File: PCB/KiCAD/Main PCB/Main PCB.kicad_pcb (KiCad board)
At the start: 2 copper layers, 120 x 120 mm, 144 parts, among them IC1 ADG608BRZ, IC2 ADG608BRZ, IC3 XB3-24Z8CM, J1 Conn_01x02, J2 Conn_01x02, J3 Conn_01x02, J4 Conn_Coaxial_Small, J5 Conn_01x02, J6 Conn_01x04, J7 Conn_01x04, M1 Conn_01x02_Pin, M2 Conn_01x02_Pin, M3 Conn_01x02_Pin, M4 Conn_01x02_Pin, Q1 BSS138, Q2 BSS138, U2 Teensy4.1, U3 Teensy4.0, U4 LMD18200, U5 LMD18200, U6 LMD18200, U7 LMD18200, U8 MIC5219-3.3YM5

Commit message: Updated to main PCB
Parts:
- added J8: Conn_01x04, Connector_JST:JST_PH_B4B-PH-K_1x04_P2.00mm_Vertical, F.Cu at (29.0, 14.5)
- turned D10 to 158 degrees
- turned D12 to 113 degrees
- turned D14 to 68 degrees
- turned D16 to 23 degrees
- turned D18 to -22 degrees
- turned D20 to -67 degrees
- turned D22 to -112 degrees
- turned D24 to -157 degrees
- turned IR10 to -22 degrees
- turned IR12 to -67 degrees
- turned IR14 to -112 degrees
- turned IR16 to -157 degrees
- turned IR2 to 158 degrees
- turned IR4 to 113 degrees
- turned IR6 to 68 degrees
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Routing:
- net GND: track 77.1 -> 964.7 mm, vias 0 -> 1
- net TSSP_PWR: track 0.00 -> 410.8 mm, vias 0 -> 4
- net +3V3: track 0.00 -> 215.3 mm, vias 0 -> 6
- net +5V: track 0.00 -> 163.3 mm, vias 0 -> 3
- net IR_DIR_157.5: track 0.00 -> 158.9 mm, vias 0 -> 3
- net LG_RECEIVE: track 0.00 -> 154.4 mm, vias 0 -> 6
- net +3V3_4_0: track 0.00 -> 147.1 mm, vias 0 -> 8
- net START_BUTTON: track 0.00 -> 137.2 mm, vias 0 -> 2
- net LED_2_A2: track 0.00 -> 134.7 mm, vias 0 -> 2
- net +3V3_4_1: track 0.00 -> 132.3 mm, vias 0 -> 5
- net 3V3_SDA: track 0.00 -> 125.4 mm, vias 0 -> 3
- net IR_DIR_180: track 0.00 -> 119.8 mm, vias 0 -> 4
- net IR_DIR_112.5: track 0.00 -> 119.7 mm, vias 0 -> 1
- net 3V3_SCL: track 0.00 -> 114.6 mm, vias 0 -> 4
- net CAMERA_TX: track 0.00 -> 109.3 mm, vias 0 -> 3
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- removed copper zone on B.Cu, net GND
- removed copper zone on F.Cu, net GND

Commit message: More PCB updates
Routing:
- net START_BUTTON: track 137.2 -> 136.2 mm
- net Net-(IC1-S1): track 55.2 -> 55.9 mm
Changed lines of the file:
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@@
 	)
 	(segment
-		(start -6.6409 7.9077)
-		(end -6.7522 8.019)
+		(start -6.75 7.75)
+		(end -7 8)
 		(width 0.2)
 		(layer "F.Cu")
@@
 	)
 	(segment
-		(start -4.8253 15.3253)
-		(end -3.75 14.25)
+		(start -4.8253 27.3847)
+		(end -4.8253 15.3253)
 		(width 0.2)
 		(layer "F.Cu")
@@
 	)
 	(segment
-		(start -3.75 14.25)
-		(end -3.75 9.0079)
+		(start -6.77 9.73)
+		(end -7 9.5)
 		(width 0.2)
 		(layer "F.Cu")
@@
 	)
 	(segment
-		(start -4.8253 27.3847)
-		(end -4.8253 15.3253)
+		(start 2.54 54.55)
+		(end 2.54 34.75)
 		(width 0.2)
 		(layer "F.Cu")
@@
 	)
 	(segment
-		(start -6.7522 9.73)
-		(end -5.788 9.73)
+		(start 2.54 34.75)
+		(end -4.8253 27.3847)
 		(width 0.2)
 		(layer "F.Cu")
@@
 	)
 	(segment
-		(start -4.8502 7.9077)
-		(end -6.6409 7.9077)
+		(start -3.75 8.75)
+		(end -4.75 7.75)
 		(width 0.2)
 		(layer "F.Cu")
@@
 	)
 	(segment
-		(start -3.75 9.0079)
-		(end -4.8502 7.9077)
+		(start -5.788 9.73)
+		(end -6.77 9.73)
 		(width 0.2)
 		(layer "F.Cu")
@@
 	)
 	(segment
-		(start 2.54 34.75)
-		(end -4.8253 27.3847)
+		(start -3.75 14.25)
+		(end -3.75 8.75)
 		(width 0.2)
 		(layer "F.Cu")
@@
 	)
 	(segment
-		(start 2.54 54.55)
-		(end 2.54 34.75)
+		(start -7 8)
+		(end -7 9.5)
+		(width 0.2)
+		(layer "F.Cu")
+		(net 17)
+	)
+	(segment
+		(start -4.8253 15.3253)
+		(end -3.75 14.25)
 		(width 0.2)
 		(layer "F.Cu")
@@
 	)
 	(segment
-		(start -6.7522 8.019)
-		(end -6.7522 9.73)
+		(start -4.75 7.75)
+		(end -6.75 7.75)
 		(width 0.2)
 		(layer "F.Cu")
@@
 	)
 	(segment
-		(start 9.6074 -6.0644)
-		(end 9.6074 -3.5)
+		(start 13.44 6)
+		(end 9.6074 6)
 		(width 0.2)
 		(layer "B.Cu")
@@
 	)
 	(segment
-		(start 10.3933 6.7859)
-		(end 9.6074 6)
+		(start 9.6074 -6.0644)
+		(end 9.6074 -3.5)
 		(width 0.2)
 		(layer "B.Cu")
@@
 	)
 	(segment
-		(start 14.2259 6.7859)
-		(end 10.3933 6.7859)
+		(start 17.75 -48.6127)
+		(end 17.8099 -48.6726)
 		(width 0.2)
 		(layer "B.Cu")
@@
 	(segment
 		(start 15.75 8.31)
-		(end 14.2259 6.7859)
-		(width 0.2)
-		(layer "B.Cu")
-		(net 54)
-	)
-	(segment
-		(start 17.75 -48.6127)
-		(end 17.8099 -48.6726)
+		(end 13.44 6)
 		(width 0.2)
 		(layer "B.Cu")
@@
 	)
 	(segment
-		(start -23.4375 11.0625)
-		(end -19.5 11.0625)
-		(width 0.68)
-		(layer "B.Cu")
-		(net 70)
-	)
-	(segment
-		(start -24.7 9.8)
-		(end -23.4375 11.0625)
+		(start -37.5 11)
+		(end -39.5 13)
 		(width 0.68)
 		(layer "B.Cu")
@@
 	)
 	(segment
-		(start -37.5 11)
-		(end -39.5 13)
+		(start -23.8375 11.0625)
+		(end -19.5 11.0625)
 		(width 0.68)
 		(layer "B.Cu")
@@
 	)
 	(segment
+		(start -24.7 10.2)
+		(end -23.8375 11.0625)
+		(width 0.68)
+		(layer "B.Cu")
+		(net 70)
+	)
+	(segment
 		(start -48.0539 16.4954)
 		(end -48.0539 -12.8966)
@@
 	)
 	(segment
-		(start -1.27 35.12)
-		(end -5.5 30.89)
+		(start -7.25 23.0489)
+		(end -7.25 29.14)
 		(width 0.2)
 		(layer "F.Cu")
@@
 	)
 	(segment
-		(start -32 -42.0058)
-		(end -32 -40)
+		(start -7.25 29.14)
+		(end -1.27 35.12)
 		(width 0.2)
 		(layer "F.Cu")
@@
 	)
 	(segment
-		(start -5.5 30.89)
-		(end -5.5 23.0489)
+		(start -32 -42.0058)
+		(end -32 -40)
 		(width 0.2)
 		(layer "F.Cu")
@@
 	)
 	(via
-		(at -5.5 23.0489)
+		(at -7.25 23.0489)
 		(size 0.554)
 		(drill 0.3)
@@
 	)
 	(segment
-		(start -49.1899 18.3796)
-		(end -48.8136 18.0033)
+		(start -48.8964 19.0881)
+		(end -49.1899 18.7946)
 		(width 0.2)
 		(layer "B.Cu")
@@
 	)
 	(segment
-		(start -28.4869 23.0489)
-		(end -32.4477 19.0881)
+		(start -49.1899 18.7946)
+		(end -49.1899 18.3796)
 		(width 0.2)
 		(layer "B.Cu")
@@
 	)
 	(segment
-		(start -49.1899 18.7946)
-		(end -49.1899 18.3796)
+		(start -49.1899 18.3796)
+		(end -48.8136 18.0033)
 		(width 0.2)
 		(layer "B.Cu")
@@
 	)
 	(segment
-		(start -32.4477 19.0881)
-		(end -48.8964 19.0881)
+		(start -7.25 23.0489)
+		(end -28.4869 23.0489)
 		(width 0.2)
 		(layer "B.Cu")
@@
 	)
 	(segment
-		(start -5.5 23.0489)
-		(end -28.4869 23.0489)
+		(start -28.4869 23.0489)
+		(end -32.4477 19.0881)
 		(width 0.2)
 		(layer "B.Cu")
@@
 	)
 	(segment
-		(start -48.8964 19.0881)
-		(end -49.1899 18.7946)
+		(start -32.4477 19.0881)
+		(end -48.8964 19.0881)
 		(width 0.2)
 		(layer "B.Cu")
@@
 	)
 	(segment
-		(start -38 -11)
-		(end -39.5 -12.5)
+		(start -24.7 -10.2)
+		(end -23.8375 -11.0625)
 		(width 0.68)
 		(layer "B.Cu")
@@
 	)
 	(segment
-		(start -23.4375 -11.0625)
-		(end -19.5 -11.0625)
+		(start -38 -11)
+		(end -39.5 -12.5)
 		(width 0.68)
 		(layer "B.Cu")
@@
 	)
 	(segment
-		(start -25.5 -11)
-		(end -38 -11)
+		(start -23.8375 -11.0625)
+		(end -19.5 -11.0625)
 		(width 0.68)
 		(layer "B.Cu")
@@
 	)
 	(segment
-		(start -24.7 -9.8)
-		(end -24.7 -10.2)
+		(start -25.5 -11)
+		(end -38 -11)
 		(width 0.68)
 		(layer "B.Cu")
@@
 	(segment
 		(start -24.7 -9.8)
-		(end -23.4375 -11.0625)
+		(end -24.7 -10.2)
 		(width 0.68)
 		(layer "B.Cu")
@@
 	)
 	(segment
-		(start 24.7 -9.8)
-		(end 23.4375 -11.0625)
+		(start 23.8375 -11.0625)
+		(end 19.5 -11.0625)
 		(width 0.68)
 		(layer "B.Cu")
@@
 	)
 	(segment
-		(start 23.4375 -11.0625)
-		(end 19.5 -11.0625)
+		(start 24.7 -10.2)
+		(end 23.8375 -11.0625)
 		(width 0.68)
 		(layer "B.Cu")

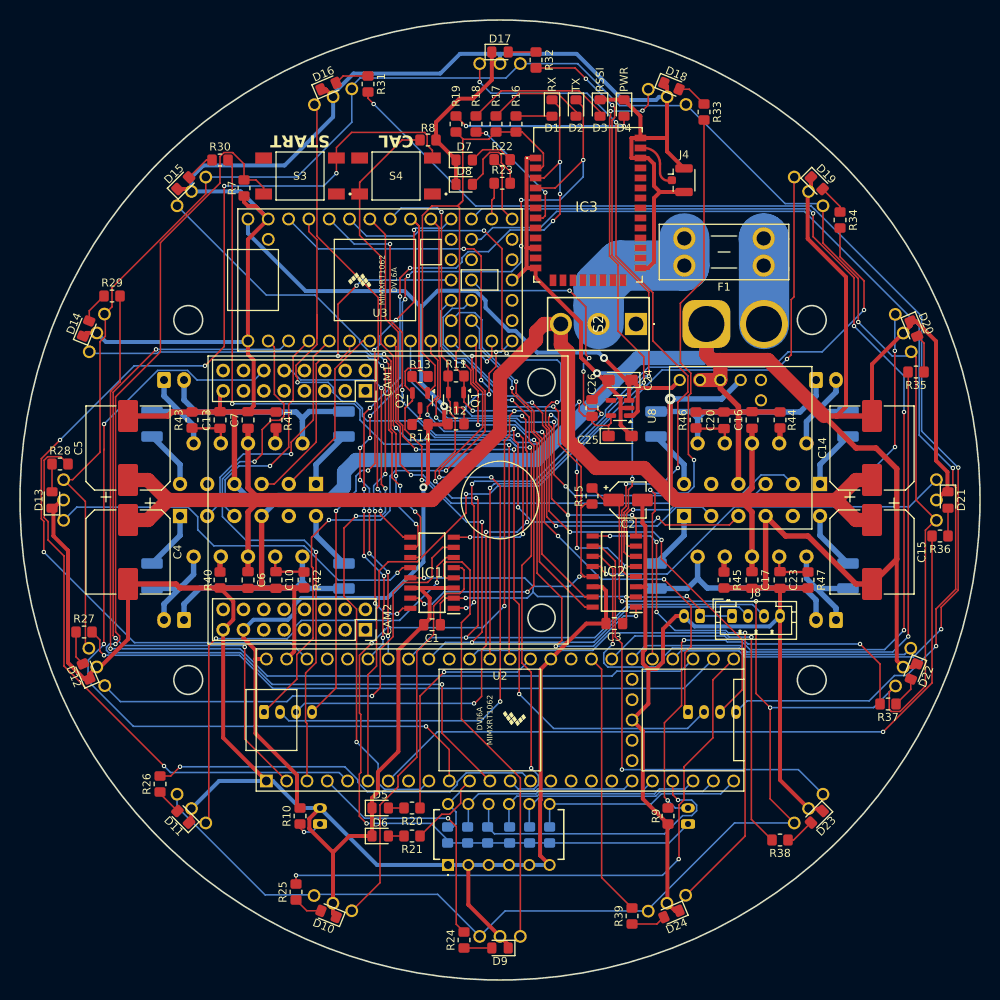
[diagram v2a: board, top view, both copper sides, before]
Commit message: The Main PCB is now curved
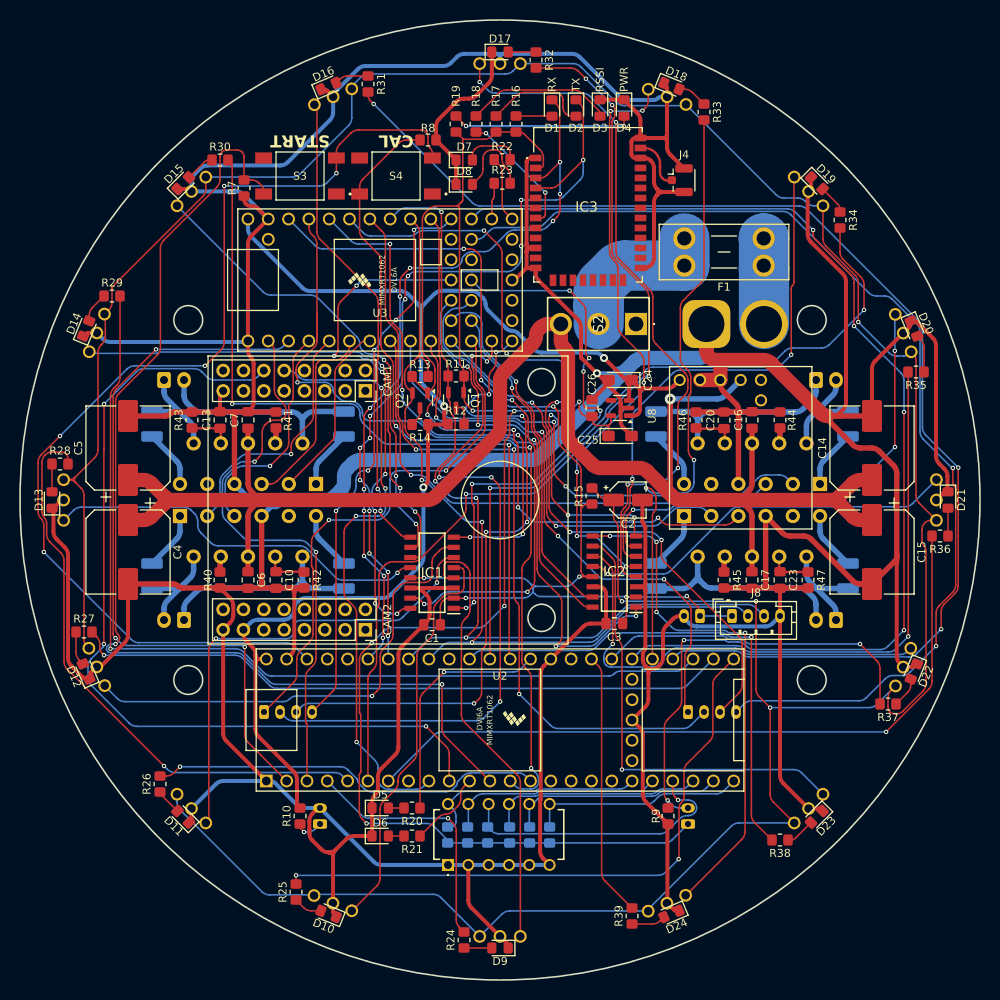
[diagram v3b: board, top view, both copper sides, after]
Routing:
- net 3V3_SDA: track 125.4 -> 107.2 mm
- net GND: track 964.7 -> 975.3 mm
- net +5V: track 163.3 -> 165.9 mm
- net +12V: track 198.6 -> 201.0 mm
- net LG_RECEIVE: track 154.4 -> 152.4 mm
- net Net-(D7-A): track 5.76 -> 7.26 mm
- net Net-(IC2-S3): track 65.7 -> 64.3 mm
- net Net-(IC2-S2): track 75.3 -> 73.8 mm
- net IR_DIR_157.5: track 158.9 -> 157.6 mm
- net CALIBRATE_BUTTON: track 107.8 -> 106.6 mm
- net CAMERA_TX: track 109.3 -> 110.5 mm
- net Net-(IC1-S6): track 65.1 -> 64.0 mm
- net +3V3_4_0: track 147.1 -> 148.1 mm
- net LED_2_A2: track 134.7 -> 133.7 mm
- net MOTOR_4_SPEED: track 61.3 -> 60.3 mm
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
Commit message: More work done to the new design
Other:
- board size 120 x 120 mm -> 118 x 118 mm
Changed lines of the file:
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@@
 		(net 162)
 	)
-	(gr_line
-		(start 8.5 18)
-		(end 8.5 -18)
+	(gr_rect
+		(start -36.5 -18)
+		(end 8.5 18)
 		(stroke
 			(width 0.1)
 			(type default)
 		)
+		(fill no)
 		(layer "F.SilkS")
 	)
@@
 		(layer "F.SilkS")
 	)
-	(gr_line
-		(start -36.5 -18)
-		(end -36.5 18)
-		(stroke
-			(width 0.1)
-			(type default)
-		)
-		(layer "F.SilkS")
-	)
-	(gr_line
-		(start 8.5 -18)
-		(end -36.5 -18)
-		(stroke
-			(width 0.1)
-			(type default)
-		)
-		(layer "F.SilkS")
-	)
-	(gr_line
-		(start -36.5 18)
-		(end 8.5 18)
-		(stroke
-			(width 0.1)
-			(type default)
-		)
-		(layer "F.SilkS")
-	)
 	(gr_circle
-		(center 38.971138 -22.500009)
-		(end 40.771138 -22.500009)
+		(center 45.730829 -30.556363)
+		(end 47.530829 -30.556363)
 		(stroke
 			(width 0.2)
@@
 	)
 	(gr_circle
-		(center 38.971138 22.500009)
-		(end 40.771138 22.500009)
+		(center 5.19 -14.73)
+		(end 6.89 -14.73)
 		(stroke
 			(width 0.2)
@@
 	)
 	(gr_circle
-		(center 5.19 14.73)
-		(end 6.89 14.73)
+		(center -45.730829 -30.556363)
+		(end -43.930829 -30.556363)
 		(stroke
 			(width 0.2)
@@
 	)
 	(gr_circle
-		(center 5.19 -14.73)
-		(end 6.89 -14.73)
+		(center 0 0)
+		(end 59 0)
 		(stroke
 			(width 0.2)
@@
 	)
 	(gr_circle
-		(center -38.971146 -22.499995)
-		(end -37.171146 -22.499995)
+		(center -45.730829 30.556363)
+		(end -43.930829 30.556363)
 		(stroke
 			(width 0.2)
@@
 	)
 	(gr_circle
-		(center 0 0)
-		(end 60 0)
+		(center 45.730829 30.556363)
+		(end 47.530829 30.556363)
 		(stroke
 			(width 0.2)
@@
 	)
 	(gr_circle
-		(center -38.971146 22.499995)
-		(end -37.171146 22.499995)
+		(center 5.19 14.73)
+		(end 6.89 14.73)
 		(stroke
 			(width 0.2)
@@
 		(layer "User.7")
 	)
-	(gr_line
-		(start 20 65)
-		(end 20 -65)
-		(stroke
-			(width 0.1)
-			(type default)
-		)
-		(layer "User.9")
-	)
-	(gr_line
+	(gr_rect
 		(start -20 -65)
-		(end -20 65)
-		(stroke
-			(width 0.1)
-			(type default)
-		)
-		(layer "User.9")
-	)
-	(gr_line
-		(start -20 65)
 		(end 20 65)
 		(stroke
 			(width 0.1)
-			(type default)
-		)
-		(layer "User.9")
-	)
-	(gr_line
-		(start -20 -65)
-		(end 20 -65)
-		(stroke
-			(width 0.1)
 			(type solid)
 		)
+		(fill no)
 		(layer "User.9")
 	)
@@
 		(polygon
 			(pts
-				(xy 36.5 20) (xy 36.5 25) (xy 41.5 25) (xy 41.5 20)
+				(xy 43.25 28) (xy 43.25 33) (xy 48.25 33) (xy 48.25 28)
 			)
 		)
@@
 		(polygon
 			(pts
-				(xy -41.5 -25) (xy -41.5 -20) (xy -36.5 -20) (xy -36.5 -25)
+				(xy -48.25 -33.25) (xy -48.25 -28.25) (xy -43.25 -28.25) (xy -43.25 -33.25)
 			)
 		)
@@
 		(polygon
 			(pts
-				(xy 36.5 -25) (xy 36.5 -20) (xy 41.5 -20) (xy 41.5 -25)
+				(xy 43.25 -33.25) (xy 43.25 -28.25) (xy 48.25 -28.25) (xy 48.25 -33.25)
 			)
 		)
@@
 		(polygon
 			(pts
-				(xy -41.5 25) (xy -36.5 25) (xy -36.5 20) (xy -41.5 20)
+				(xy -48.25 33) (xy -43.25 33) (xy -43.25 28) (xy -48.25 28)
 			)
 		)
 	)
 	(group ""
-		(members "486d49f0-5f72-47ae-aaa7-721b27d75e4e" "4ed6d5d1-6411-429f-8d68-8ec70c6e130c"
-			"5f59e99a-3ac1-4652-a327-1dbe7bcba340" "7fa5b84a-e179-4130-818b-b4899d309634"
-			"a3d77582-7e22-4d04-964b-be2d7a1d58ef" "d20a5f4b-9604-4b83-9d09-14cad19127cd"
-			"e6d5e6d5-4d51-463c-a5db-a39310c9b900"
+		(members "424606c2-0dc2-4a65-b47a-a76d804a3286" "48313cfd-0571-48b8-92fb-89c092793adc"
+			"4d94b3ce-4b71-4596-a857-ba8f6752f409" "5c8ab7ad-c14e-42ee-bad5-365819e6007c"
+			"6529d427-8057-4534-8c0a-2f980f93bae1" "6af3e00f-15df-492b-a6eb-79ff3be3cb8a"
+			"8f6581ea-ed91-4ff0-942c-d67ddc84d4b2"
 		)
 	)
